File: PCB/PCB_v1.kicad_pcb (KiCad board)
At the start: 2 copper layers, 80 x 40 mm, 11 parts, among them J1 Accelerometer, J2 Flysky FS2A Receiver, J3 DC-DC, J4 Battery Left, J5 Battery Right, J6 ESC_Left, J7 ESC_Right, U1 Teensy4.0

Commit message: Update PCB Appearance
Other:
- board text added: "(PCB Center)"
- board text added: "80mm × 40mm"
- board text added: "B.Cu 3 oz (105 μm)"
- board text added: "F.Cu 1 oz (35 μm)"
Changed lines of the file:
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@@
 		(allow_soldermask_bridges_in_footprints no)
 		(tenting front back)
+		(grid_origin 180 80)
 		(pcbplotparams
 			(layerselection 0x00000000_00000000_55555555_5755f5ff)
@@
 		(layer "F.SilkS")
 	)
+	(gr_line
+		(start 180 80)
+		(end 180 72)
+		(stroke
+			(width 0.1)
+			(type default)
+		)
+		(layer "B.SilkS")
+	)
+	(gr_line
+		(start 180 80)
+		(end 188 80)
+		(stroke
+			(width 0.1)
+			(type default)
+		)
+		(layer "B.SilkS")
+	)
+	(gr_circle
+		(center 180 80)
+		(end 180.3 80)
+		(stroke
+			(width 0.1)
+			(type solid)
+		)
+		(fill no)
+		(layer "B.SilkS")
+	)
+	(gr_line
+		(start 180 72)
+		(end 181 73)
+		(stroke
+			(width 0.1)
+			(type default)
+		)
+		(layer "B.SilkS")
+	)
+	(gr_line
+		(start 188 80)
+		(end 187 79)
+		(stroke
+			(width 0.1)
+			(type default)
+		)
+		(layer "B.SilkS")
+	)
+	(gr_line
+		(start 188 80)
+		(end 187 81)
+		(stroke
+			(width 0.1)
+			(type default)
+		)
+		(layer "B.SilkS")
+	)
+	(gr_line
+		(start 180 72)
+		(end 179 73)
+		(stroke
+			(width 0.1)
+			(type default)
+		)
+		(layer "B.SilkS")
+	)
 	(gr_rect
 		(start 140 60)
@@
 		)
 	)
+	(gr_text "F.Cu  1 oz (35 μm)"
+		(at 200 66 0)
+		(layer "F.SilkS")
+		(effects
+			(font
+				(size 0.5 0.5)
+				(thickness 0.1)
+			)
+			(justify bottom)
+		)
+	)
 	(gr_text "Battery"
 		(at 158.9 67 0)
@@
 			)
 			(justify left bottom)
+		)
+	)
+	(gr_text "80mm × 40mm"
+		(at 219 99 0)
+		(layer "F.SilkS")
+		(effects
+			(font
+				(size 1 1)
+				(thickness 0.1)
+			)
+			(justify right)
 		)
 	)
@@
 		)
 	)
+	(gr_text "x"
+		(at 186 81 -0)
+		(layer "B.SilkS")
+		(effects
+			(font
+				(size 1 1)
+				(thickness 0.1)
+			)
+			(justify mirror)
+		)
+	)
+	(gr_text "y"
+		(at 182 73 0)
+		(layer "B.SilkS")
+		(effects
+			(font
+				(size 1 1)
+				(thickness 0.1)
+			)
+			(justify mirror)
+		)
+	)
+	(gr_text "(PCB Center)"
+		(at 180 81 0)
+		(layer "B.SilkS")
+		(effects
+			(font
+				(size 0.5 0.5)
+				(thickness 0.1)
+			)
+			(justify bottom mirror)
+		)
+	)
 	(gr_text "Bottom Layer"
 		(at 200.025 63.5 -0)
@@
 		)
 	)
+	(gr_text "B.Cu  3 oz (105 μm)"
+		(at 200 66 0)
+		(layer "B.SilkS")
+		(effects
+			(font
+				(size 0.5 0.5)
+				(thickness 0.1)
+			)
+			(justify bottom mirror)
+		)
+	)

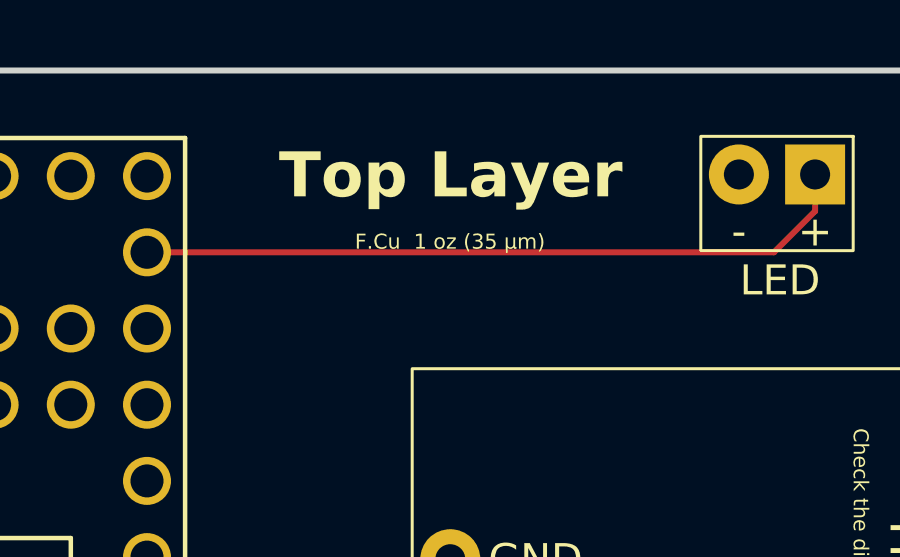
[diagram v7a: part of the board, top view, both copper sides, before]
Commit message: Change the Text on Silkscreen
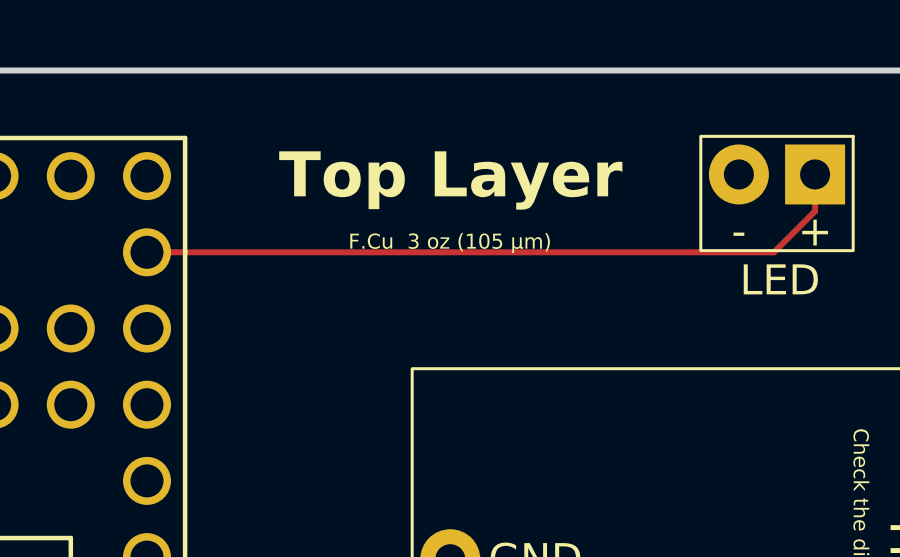
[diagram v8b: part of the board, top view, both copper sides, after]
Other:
- board text added: "B.Cu 1 oz (35 μm)"
- board text added: "F.Cu 3 oz (105 μm)"
- board text removed: "B.Cu 3 oz (105 μm)"
- board text removed: "F.Cu 1 oz (35 μm)"
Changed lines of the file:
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@@
 		)
 	)
-	(gr_text "F.Cu  1 oz (35 μm)"
+	(gr_text "F.Cu  3 oz (105 μm)"
 		(at 200 66 0)
 		(layer "F.SilkS")
@@
 		)
 	)
-	(gr_text "B.Cu  3 oz (105 μm)"
+	(gr_text "B.Cu  1 oz (35 μm)"
 		(at 200 66 0)
 		(layer "B.SilkS")
